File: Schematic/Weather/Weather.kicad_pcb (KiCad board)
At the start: 2 copper layers, 38 parts, among them J1 4_Way_Wire, J2 3_Way_Wire, J3 3_Way_Wire, Q1 BSS138, Q2 AO3401, Q3 AO3401, U1 AMS1117, U2 ESP-01v090, U3 AMS1117, U4 ESP-01v090, U5 LM321

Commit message: more board layouts
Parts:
- added C5: 0.1uF, Capacitor_THT:C_Disc_D3.8mm_W2.6mm_P2.50mm, F.Cu at (-3.85, -160.0)
- added D3: in916, Diode_THT:D_DO-35_SOD27_P2.54mm_Vertical_KathodeUp, F.Cu at (-6.35, -154.9)
- added D4: in916, Diode_THT:D_DO-35_SOD27_P2.54mm_Vertical_AnodeUp, F.Cu at (-3.81, -157.5)
- added H1: MountingHole_Pad, Connector_Wire:SolderWirePad_1x01_Drill0.8mm, F.Cu at (20.3, -137.2)
- added H2: MountingHole_Pad, Connector_Wire:SolderWirePad_1x01_Drill0.8mm, F.Cu at (20.3, -113.0)
- added H3: MountingHole_Pad, Connector_Wire:SolderWirePad_1x01_Drill0.8mm, F.Cu at (20.3, -132.1)
- added H4: MountingHole_Pad, Connector_Wire:SolderWirePad_1x01_Drill0.8mm, F.Cu at (20.3, -119.4)
- added H5: MountingHole_Pad, Connector_Wire:SolderWirePad_1x01_Drill0.8mm, F.Cu at (-1.27, -154.9)
- added H6: MountingHole_Pad, Connector_Wire:SolderWirePad_1x01_Drill0.8mm, F.Cu at (-1.27, -170.2)
- added H7: MountingHole_Pad, Connector_Wire:SolderWirePad_1x01_Drill0.8mm, F.Cu at (-1.27, -158.8)
- added H8: MountingHole_Pad, Connector_Wire:SolderWirePad_1x01_Drill0.8mm, F.Cu at (-1.27, -166.4)
- added J4: 3_Way_Wire, Connector_PinHeader_2.54mm:PinHeader_1x03_P2.54mm_Vertical, F.Cu at (-16.5, -172.7)
- added J5: 3_Way_Wire, Connector_PinHeader_2.54mm:PinHeader_1x03_P2.54mm_Vertical, F.Cu at (-16.5, -152.4)
- added Q4: BSS138, Package_TO_SOT_SMD:SOT-23, F.Cu at (-7.62, -172.7)
- added Q5: AO3401, Package_TO_SOT_SMD:SOT-23, F.Cu at (-2.54, -168.9)
- added Q6: AO3401, Package_TO_SOT_SMD:SOT-23, F.Cu at (-7.62, -167.6)
- added R17: 2.2K, Resistor_THT:R_Axial_DIN0204_L3.6mm_D1.6mm_P2.54mm_Vertical, F.Cu at (-11.4, -172.7)
- added R18: 4.7K, Resistor_THT:R_Axial_DIN0204_L3.6mm_D1.6mm_P2.54mm_Vertical, F.Cu at (-14.0, -160.0)
- added R19: 2.2k, Resistor_THT:R_Axial_DIN0204_L3.6mm_D1.6mm_P2.54mm_Vertical, F.Cu at (-1.27, -172.7)
- added R20: 5.1K, Resistor_THT:R_Axial_DIN0204_L3.6mm_D1.6mm_P2.54mm_Vertical, F.Cu at (-16.5, -165.1)
- added R21: 4.7K, Resistor_THT:R_Axial_DIN0204_L3.6mm_D1.6mm_P2.54mm_Vertical, F.Cu at (-8.89, -160.0)
- added R22: 10K, Resistor_THT:R_Axial_DIN0204_L3.6mm_D1.6mm_P2.54mm_Vertical, F.Cu at (-6.35, -170.2)
- added R23: 4.7K, Resistor_THT:R_Axial_DIN0204_L3.6mm_D1.6mm_P2.54mm_Vertical, F.Cu at (-11.4, -154.9)
- added R24: 4.7K, Resistor_THT:R_Axial_DIN0204_L3.6mm_D1.6mm_P2.54mm_Vertical, F.Cu at (-8.89, -152.4)
- added R25: 4.7K, Resistor_THT:R_Axial_DIN0204_L3.6mm_D1.6mm_P2.54mm_Vertical, F.Cu at (-8.89, -157.5)
- added R26: 20K, Resistor_THT:R_Axial_DIN0204_L3.6mm_D1.6mm_P2.54mm_Vertical, F.Cu at (-3.81, -165.1)
- added R27: 20K, Resistor_THT:R_Axial_DIN0204_L3.6mm_D1.6mm_P2.54mm_Vertical, F.Cu at (-11.4, -170.2)
- added R28: 680, Resistor_THT:R_Axial_DIN0204_L3.6mm_D1.6mm_P2.54mm_Vertical, F.Cu at (-8.89, -165.1)
- added R29: 47K, Resistor_THT:R_Axial_DIN0204_L3.6mm_D1.6mm_P2.54mm_Vertical, F.Cu at (-14.0, -167.6)
- added R30: 3.3k, Resistor_THT:R_Axial_DIN0204_L3.6mm_D1.6mm_P2.54mm_Vertical, F.Cu at (-1.27, -152.4)
- added U6: LM321, Package_TO_SOT_SMD:SOT-23-5, F.Cu at (-12.7, -157.5)
- moved J2 6.35 mm to (1.27, -113.0), turned to 180 degrees
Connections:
- net /Anenometer Control Board/J13_P2 renamed /North Sensor/J17_P2
- net /Anenometer Control Board/J13_P3 renamed /North Sensor/J17_P3
- net /Anenometer Control Board/J13_P4 renamed /North Sensor/J17_P4
- net /Anenometer Control Board/J13_P5 renamed /North Sensor/J17_P5
- net GNDS renamed /North Sensor/J17_P1
- net Vdrive renamed Net-(H1-Pad1)
- J1 pad 1: Net-(J1-Pad1) -> (no net)
- J1 pad 2: Net-(J1-Pad2) -> (no net)
- J1 pad 3: Net-(J1-Pad3) -> (no net)
- J1 pad 4: Net-(J1-Pad4) -> (no net)
- PSU2 pad 2: /PSU 2/J5_P2 -> (no net)
- PSU3 pad 2: /PSU 2/J5_P3 -> (no net)
- U2 pad 1: Net-(U2-Pad1) -> (no net)
- U2 pad 8: Net-(U2-Pad8) -> (no net)
- U3 pad 3: Net-(U3-Pad3) -> (no net)
- U4 pad 1: Net-(U4-Pad1) -> (no net)
- U4 pad 3: Net-(U4-Pad3) -> (no net)
- U4 pad 4: Net-(U4-Pad4) -> (no net)
- U4 pad 5: Net-(U4-Pad5) -> (no net)
- U4 pad 6: Net-(U4-Pad6) -> (no net)
- U4 pad 8: Net-(U4-Pad8) -> (no net)
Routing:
- net GNDS: track 0.00 -> 62.2 mm
- net /Anenometer Control Board/J14_P4: track 0.00 -> 25.9 mm
- net Net-(H5-Pad1): track 0.00 -> 24.2 mm
- net Net-(Q6-Pad1): track 0.00 -> 23.3 mm
- net Net-(Q4-Pad1): track 0.00 -> 13.6 mm
- net /Anenometer Control Board/J14_P5: track 0.00 -> 10.9 mm
- net Net-(C5-Pad1): track 0.00 -> 7.64 mm
- net Net-(R21-Pad1): track 0.00 -> 7.52 mm
- net Net-(Q5-Pad1): track 0.00 -> 7.02 mm
- net Net-(R23-Pad1): track 0.00 -> 5.25 mm
- net Net-(R18-Pad1): track 0.00 -> 4.20 mm
- net /Anenometer Control Board/J14_P2: track 0.00 -> 4.20 mm
- net Net-(C5-Pad2): track 0.00 -> 3.59 mm
- net Net-(Q4-Pad3): track 0.00 -> 3.48 mm
- net Net-(Q6-Pad3): track 0.00 -> 2.65 mm
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
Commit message: More boards added
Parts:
- added C6: 0.1uF, Capacitor_THT:C_Disc_D3.8mm_W2.6mm_P2.50mm, F.Cu at (44.5, -142.9)
- added C7: 0.1uF, Capacitor_THT:C_Disc_D3.8mm_W2.6mm_P2.50mm, F.Cu at (95.2, -169.3)
- added D5: in916, Diode_THT:D_DO-35_SOD27_P2.54mm_Vertical_KathodeUp, F.Cu at (32.5, -143.1)
- added D6: in916, Diode_THT:D_DO-35_SOD27_P2.54mm_Vertical_AnodeUp, F.Cu at (38.8, -143.1)
- added D7: in916, Diode_THT:D_DO-35_SOD27_P2.54mm_Vertical_KathodeUp, F.Cu at (83.2, -169.5)
- added D8: in916, Diode_THT:D_DO-35_SOD27_P2.54mm_Vertical_AnodeUp, F.Cu at (89.6, -169.5)
- added H10: MountingHole_Pad, Connector_Wire:SolderWirePad_1x01_Drill0.8mm, F.Cu at (58.2, -131.2)
- added H11: MountingHole_Pad, Connector_Wire:SolderWirePad_1x01_Drill0.8mm, F.Cu at (58.6, -135.2)
- added H12: MountingHole_Pad, Connector_Wire:SolderWirePad_1x01_Drill0.8mm, F.Cu at (54.1, -131.0)
- added H13: MountingHole_Pad, Connector_Wire:SolderWirePad_1x01_Drill0.8mm, F.Cu at (109.0, -157.7)
- added H14: MountingHole_Pad, Connector_Wire:SolderWirePad_1x01_Drill0.8mm, F.Cu at (109.4, -161.7)
- added H15: MountingHole_Pad, Connector_Wire:SolderWirePad_1x01_Drill0.8mm, F.Cu at (104.9, -157.4)
- added H16: MountingHole_Pad, Connector_Wire:SolderWirePad_1x01_Drill0.8mm, F.Cu at (105.3, -161.7)
- added H9: MountingHole_Pad, Connector_Wire:SolderWirePad_1x01_Drill0.8mm, F.Cu at (54.5, -135.2)
- added J6: 3_Way_Wire, Connector_PinHeader_2.54mm:PinHeader_1x03_P2.54mm_Vertical, F.Cu at (28.6, -142.6)
- added J7: 3_Way_Wire, Connector_PinHeader_2.54mm:PinHeader_1x03_P2.54mm_Vertical, F.Cu at (28.6, -132.9)
- added J8: 3_Way_Wire, Connector_PinHeader_2.54mm:PinHeader_1x03_P2.54mm_Vertical, F.Cu at (79.3, -169.1)
- added J9: 3_Way_Wire, Connector_PinHeader_2.54mm:PinHeader_1x03_P2.54mm_Vertical, F.Cu at (80.0, -159.4)
- added Q10: BSS138, Package_TO_SOT_SMD:SOT-23, F.Cu at (100.7, -157.2)
- added Q11: AO3401, Package_TO_SOT_SMD:SOT-23, F.Cu at (95.1, -155.6)
- added Q12: AO3401, Package_TO_SOT_SMD:SOT-23, F.Cu at (106.3, -166.0)
- added Q7: BSS138, Package_TO_SOT_SMD:SOT-23, F.Cu at (55.5, -139.5)
- added Q8: AO3401, Package_TO_SOT_SMD:SOT-23, F.Cu at (49.9, -130.7)
- added Q9: AO3401, Package_TO_SOT_SMD:SOT-23, F.Cu at (44.3, -129.1)
- added R31: 2.2K, Resistor_THT:R_Axial_DIN0204_L3.6mm_D1.6mm_P2.54mm_Vertical, F.Cu at (55.7, -143.4)
- added R32: 4.7K, Resistor_THT:R_Axial_DIN0204_L3.6mm_D1.6mm_P2.54mm_Vertical, F.Cu at (49.2, -139.2)
- added R33: 2.2k, Resistor_THT:R_Axial_DIN0204_L3.6mm_D1.6mm_P2.54mm_Vertical, F.Cu at (43.6, -136.1)
- added R34: 5.1K, Resistor_THT:R_Axial_DIN0204_L3.6mm_D1.6mm_P2.54mm_Vertical, F.Cu at (38.0, -130.2)
- added R35: 4.7K, Resistor_THT:R_Axial_DIN0204_L3.6mm_D1.6mm_P2.54mm_Vertical, F.Cu at (50.1, -143.4)
- added R36: 10K, Resistor_THT:R_Axial_DIN0204_L3.6mm_D1.6mm_P2.54mm_Vertical, F.Cu at (43.6, -132.9)
- added R37: 4.7K, Resistor_THT:R_Axial_DIN0204_L3.6mm_D1.6mm_P2.54mm_Vertical, F.Cu at (32.5, -139.6)
- added R38: 4.7K, Resistor_THT:R_Axial_DIN0204_L3.6mm_D1.6mm_P2.54mm_Vertical, F.Cu at (38.0, -133.3)
- added R39: 4.7K, Resistor_THT:R_Axial_DIN0204_L3.6mm_D1.6mm_P2.54mm_Vertical, F.Cu at (43.6, -139.2)
- added R40: 20K, Resistor_THT:R_Axial_DIN0204_L3.6mm_D1.6mm_P2.54mm_Vertical, F.Cu at (32.5, -130.2)
- added R41: 20K, Resistor_THT:R_Axial_DIN0204_L3.6mm_D1.6mm_P2.54mm_Vertical, F.Cu at (32.5, -133.3)
- added R42: 680, Resistor_THT:R_Axial_DIN0204_L3.6mm_D1.6mm_P2.54mm_Vertical, F.Cu at (38.0, -136.5)
- added R43: 47K, Resistor_THT:R_Axial_DIN0204_L3.6mm_D1.6mm_P2.54mm_Vertical, F.Cu at (32.5, -136.5)
- added R44: 3.3k, Resistor_THT:R_Axial_DIN0204_L3.6mm_D1.6mm_P2.54mm_Vertical, F.Cu at (38.0, -139.6)
- added R45: 2.2K, Resistor_THT:R_Axial_DIN0204_L3.6mm_D1.6mm_P2.54mm_Vertical, F.Cu at (88.8, -166.1)
- added R46: 4.7K, Resistor_THT:R_Axial_DIN0204_L3.6mm_D1.6mm_P2.54mm_Vertical, F.Cu at (83.2, -166.1)
- added R47: 2.2k, Resistor_THT:R_Axial_DIN0204_L3.6mm_D1.6mm_P2.54mm_Vertical, F.Cu at (83.2, -162.9)
- added R48: 5.1K, Resistor_THT:R_Axial_DIN0204_L3.6mm_D1.6mm_P2.54mm_Vertical, F.Cu at (88.8, -159.8)
- added R49: 4.7K, Resistor_THT:R_Axial_DIN0204_L3.6mm_D1.6mm_P2.54mm_Vertical, F.Cu at (94.4, -159.4)
- added R50: 10K, Resistor_THT:R_Axial_DIN0204_L3.6mm_D1.6mm_P2.54mm_Vertical, F.Cu at (88.8, -156.6)
- added R51: 4.7K, Resistor_THT:R_Axial_DIN0204_L3.6mm_D1.6mm_P2.54mm_Vertical, F.Cu at (83.2, -159.8)
- added R52: 4.7K, Resistor_THT:R_Axial_DIN0204_L3.6mm_D1.6mm_P2.54mm_Vertical, F.Cu at (94.4, -165.7)
- added R53: 4.7K, Resistor_THT:R_Axial_DIN0204_L3.6mm_D1.6mm_P2.54mm_Vertical, F.Cu at (88.8, -162.9)
- added R54: 20K, Resistor_THT:R_Axial_DIN0204_L3.6mm_D1.6mm_P2.54mm_Vertical, F.Cu at (106.5, -169.8)
- added R55: 20K, Resistor_THT:R_Axial_DIN0204_L3.6mm_D1.6mm_P2.54mm_Vertical, F.Cu at (100.0, -165.7)
- added R56: 680, Resistor_THT:R_Axial_DIN0204_L3.6mm_D1.6mm_P2.54mm_Vertical, F.Cu at (94.4, -162.6)
- added R57: 47K, Resistor_THT:R_Axial_DIN0204_L3.6mm_D1.6mm_P2.54mm_Vertical, F.Cu at (83.2, -156.6)
- added R58: 3.3k, Resistor_THT:R_Axial_DIN0204_L3.6mm_D1.6mm_P2.54mm_Vertical, F.Cu at (100.9, -169.8)
- added U7: LM321, Package_TO_SOT_SMD:SOT-23-5, F.Cu at (50.1, -135.3)
- added U8: LM321, Package_TO_SOT_SMD:SOT-23-5, F.Cu at (100.9, -161.8)
- moved R3 61.8 mm to (14.0, -172.7), turned to 180 degrees
- moved Q1 60.8 mm to (17.5, -172.8), turned to 0 degrees
- moved J2 60.2 mm to (8.89, -172.7), turned to 0 degrees
- moved R5 59.5 mm to (24.1, -172.7), turned to 180 degrees
- moved H2 57.3 mm to (24.1, -170.2)
- moved Q3 55.0 mm to (17.8, -167.6), turned to 180 degrees
- moved R8 54.3 mm to (19.1, -170.2), turned to 180 degrees
- moved R14 53.4 mm to (16.5, -165.1), turned to 180 degrees
- moved R6 53.3 mm to (8.89, -165.1), turned to 0 degrees
- moved Q2 52.1 mm to (22.9, -168.9), turned to 0 degrees
- moved R13 51.4 mm to (14.0, -170.2), turned to 270 degrees
- moved R15 50.9 mm to (11.4, -167.6)
- moved H4 47.1 mm to (24.1, -166.4)
- moved R12 46.0 mm to (21.6, -165.1), turned to 180 degrees
- moved R4 29.9 mm to (11.4, -160.0)
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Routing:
- net (no net): track 0.00 -> 416.3 mm
- net /North Sensor/J17_P1: track 0.00 -> 62.2 mm
- net /North Sensor/J17_P4: track 0.00 -> 25.9 mm
- net Net-(H1-Pad1): track 0.00 -> 24.2 mm
- net Net-(Q3-Pad1): track 0.00 -> 23.3 mm
- net Net-(Q1-Pad1): track 0.00 -> 13.6 mm
- net /North Sensor/J17_P5: track 0.00 -> 10.9 mm
- net Net-(C4-Pad1): track 0.00 -> 7.64 mm
- net Net-(R11-Pad2): track 0.00 -> 7.52 mm
- net Net-(Q2-Pad1): track 0.00 -> 7.02 mm
- net Net-(R10-Pad1): track 0.00 -> 5.25 mm
- net Net-(R4-Pad1): track 0.00 -> 4.20 mm
- net /North Sensor/J17_P2: track 0.00 -> 4.20 mm
- net Net-(C4-Pad2): track 0.00 -> 3.59 mm
- net Net-(Q1-Pad3): track 0.00 -> 3.48 mm
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
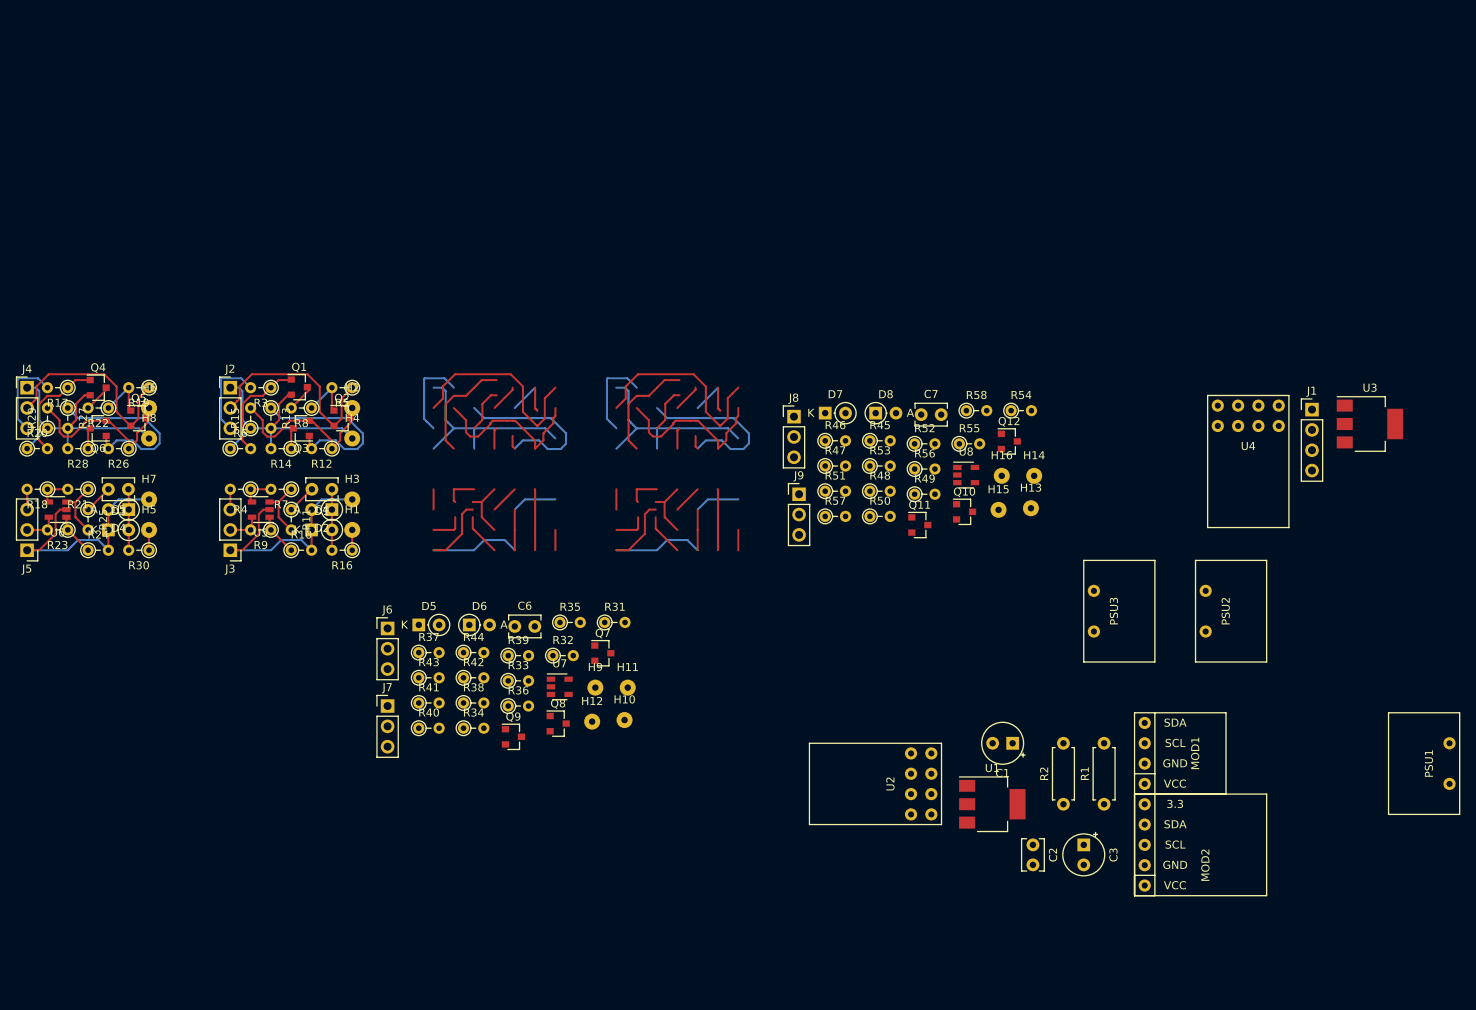
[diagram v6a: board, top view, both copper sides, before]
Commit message: Board update 4 channels
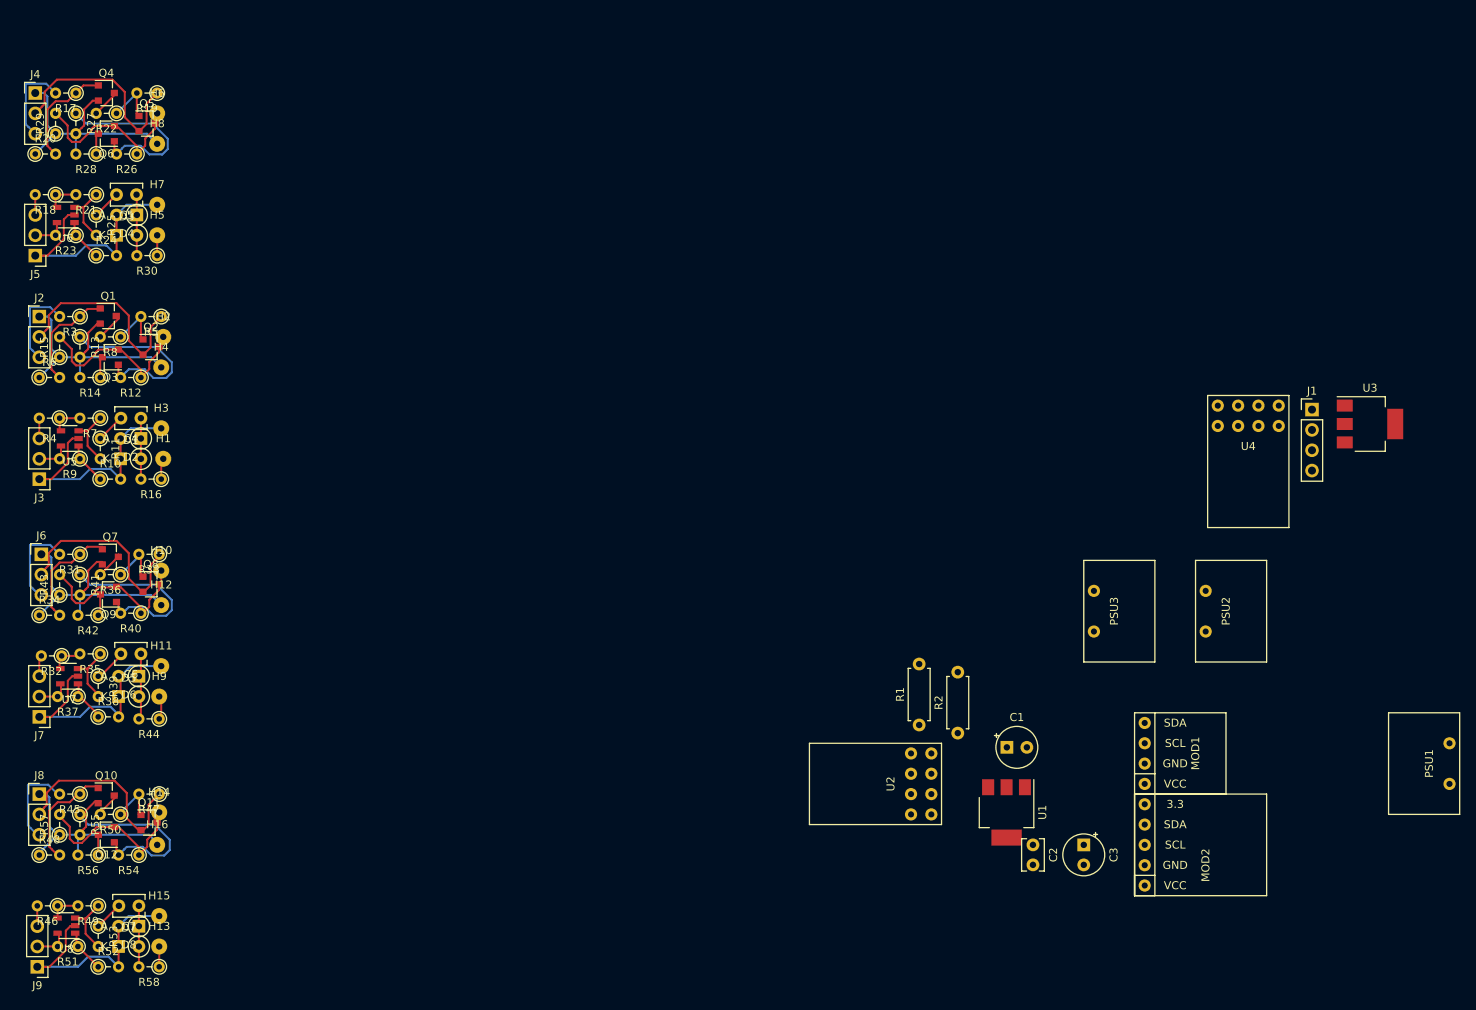
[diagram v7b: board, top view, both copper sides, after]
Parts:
- moved U8 125.8 mm to (-11.6, -105.5), turned to 180 degrees
- moved Q12 123.1 mm to (-6.60, -116.8), turned to 180 degrees
- moved R58 122.5 mm to (0.00, -100.3), turned to 180 degrees
- moved R54 122.4 mm to (-2.54, -114.3), turned to 180 degrees
- moved H13 122.0 mm to (0.00, -102.9)
- moved R52 121.2 mm to (-7.62, -100.3)
- moved R55 119.3 mm to (-9.91, -119.4), turned to 270 degrees
- moved H14 117.2 mm to (0.00, -119.6)
- moved H15 116.6 mm to (0.00, -106.7)
- moved C7 115.5 mm to (-2.54, -108.0), turned to 180 degrees
- moved H16 115.2 mm to (-0.25, -115.6)
- moved R49 114.3 mm to (-7.62, -108.0), turned to 180 degrees
- moved R48 113.4 mm to (-15.0, -114.3)
- moved Q10 113.0 mm to (-6.62, -121.7)
- moved R56 112.9 mm to (-7.62, -114.3), turned to 180 degrees
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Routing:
- net (no net): track 416.3 -> 0.00 mm
- net /Eath Sensor/J19_P1: track 0.00 -> 62.2 mm
- net /West Sensor/J20_P1: track 0.00 -> 62.2 mm
- net /West Sensor/J20_P4: track 0.00 -> 25.9 mm
- net /Eath Sensor/J19_P4: track 0.00 -> 25.9 mm
- net Net-(H13-Pad1): track 0.00 -> 24.2 mm
- net Net-(H10-Pad1): track 0.00 -> 24.2 mm
- net Net-(Q9-Pad1): track 0.00 -> 23.3 mm
- net Net-(Q12-Pad1): track 0.00 -> 23.3 mm
- net Net-(Q7-Pad1): track 0.00 -> 13.6 mm
- net Net-(Q10-Pad1): track 0.00 -> 13.6 mm
- net /Eath Sensor/J19_P5: track 0.00 -> 10.9 mm
- net /West Sensor/J20_P5: track 0.00 -> 10.9 mm
- net Net-(C7-Pad1): track 0.00 -> 7.64 mm
- net Net-(C6-Pad1): track 0.00 -> 7.64 mm
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
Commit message: new M_Board internal
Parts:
- added H17: MountingHole_Pad, Connector_Wire:SolderWirePad_1x01_Drill0.8mm, F.Cu at (90.2, -190.5)
- added H18: MountingHole_Pad, Connector_Wire:SolderWirePad_1x01_Drill0.8mm, F.Cu at (94.2, -190.5)
- added J10: Conn_02x04_Odd_Even, Connector_PinHeader_2.54mm:PinHeader_2x04_P2.54mm_Vertical, F.Cu at (83.3, -173.9)
- added J11: Conn_01x04_Female, Connector_PinHeader_2.54mm:PinHeader_1x04_P2.54mm_Vertical, F.Cu at (61.4, -190.2)
- added J12: Conn_01x05_Female, Connector_PinHeader_2.54mm:PinHeader_1x05_P2.54mm_Vertical, F.Cu at (52.1, -190.2)
- added J13: Conn_01x04_Male, Connector_PinHeader_2.54mm:PinHeader_1x04_P2.54mm_Vertical, F.Cu at (66.1, -190.2)
- added J14: Conn_01x05_Male, Connector_PinHeader_2.54mm:PinHeader_1x05_P2.54mm_Vertical, F.Cu at (56.8, -190.2)
- added J15: Conn_02x04_Odd_Even, Connector_PinHeader_2.54mm:PinHeader_2x04_P2.54mm_Vertical, F.Cu at (83.3, -190.2)
- R1: value 10k -> 4.7K
- moved C3 126.0 mm to (27.9, -206.1), turned to 0 degrees
- moved C2 120.9 mm to (41.4, -215.6), turned to 0 degrees
- moved U1 117.8 mm to (34.9, -213.5), turned to 0 degrees
- moved C1 115.5 mm to (21.3, -206.3)
- moved R2 113.9 mm to (20.8, -211.6), turned to 0 degrees
- moved R1 112.9 mm to (20.8, -215.6), turned to 0 degrees
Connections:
- C1 pad 1: /PSU 1/J1_P2 -> /Int Motherboard/J2_P2
- C1 pad 2: GND -> /Int Motherboard/J2_P1
- C2 pad 1: Net-(C2-Pad1) -> /Int Motherboard/J3_P6
- C2 pad 2: GND -> /Int Motherboard/J2_P1
- C3 pad 1: Net-(C2-Pad1) -> /Int Motherboard/J3_P6
- C3 pad 2: GND -> /Int Motherboard/J2_P1
- MOD1 pad 1: /PSU 1/J1_P2 -> (no net)
- MOD1 pad 2: GND -> (no net)
- MOD1 pad 3: /Internal ESP8266/J3_P3 -> (no net)
- MOD1 pad 4: /Internal ESP8266/J3_P2 -> (no net)
- MOD2 pad 1: /PSU 1/J1_P2 -> (no net)
- MOD2 pad 2: GND -> (no net)
- MOD2 pad 3: /Internal ESP8266/J3_P3 -> (no net)
- MOD2 pad 4: /Internal ESP8266/J3_P2 -> (no net)
- PSU1 pad 1: GND -> (no net)
- PSU1 pad 2: /PSU 1/J1_P2 -> (no net)
- R1 pad 1: Net-(C2-Pad1) -> /Int Motherboard/J3_P6
- R1 pad 2: Net-(R1-Pad2) -> (no net)
- R2 pad 1: Net-(C2-Pad1) -> /Int Motherboard/J3_P6
- R2 pad 2: Net-(R2-Pad2) -> (no net)
- U1 pad 1: GND -> /Int Motherboard/J2_P1
- U1 pad 2: Net-(C2-Pad1) -> /Int Motherboard/J3_P6
- U1 pad 3: /PSU 1/J1_P2 -> /Int Motherboard/J2_P2
- U2 pad 2: GND -> (no net)
- U2 pad 3: Net-(R2-Pad2) -> (no net)
- U2 pad 4: /Internal ESP8266/J3_P3 -> (no net)
- U2 pad 5: Net-(R1-Pad2) -> (no net)
- U2 pad 6: /Internal ESP8266/J3_P2 -> (no net)
- U2 pad 7: Net-(C2-Pad1) -> (no net)
